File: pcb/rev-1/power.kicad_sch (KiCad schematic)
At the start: 38 parts, among them J1 12402012E212A, J2 S2B-PH-SM4-TB, J6 B2B-PH-K-S, SW1 EVQPUD02K, U1 NUF2042XV6T1G, U2 RT6160AWSC, U3 KTS1662EUW-TR, U4 BQ25150YFPR

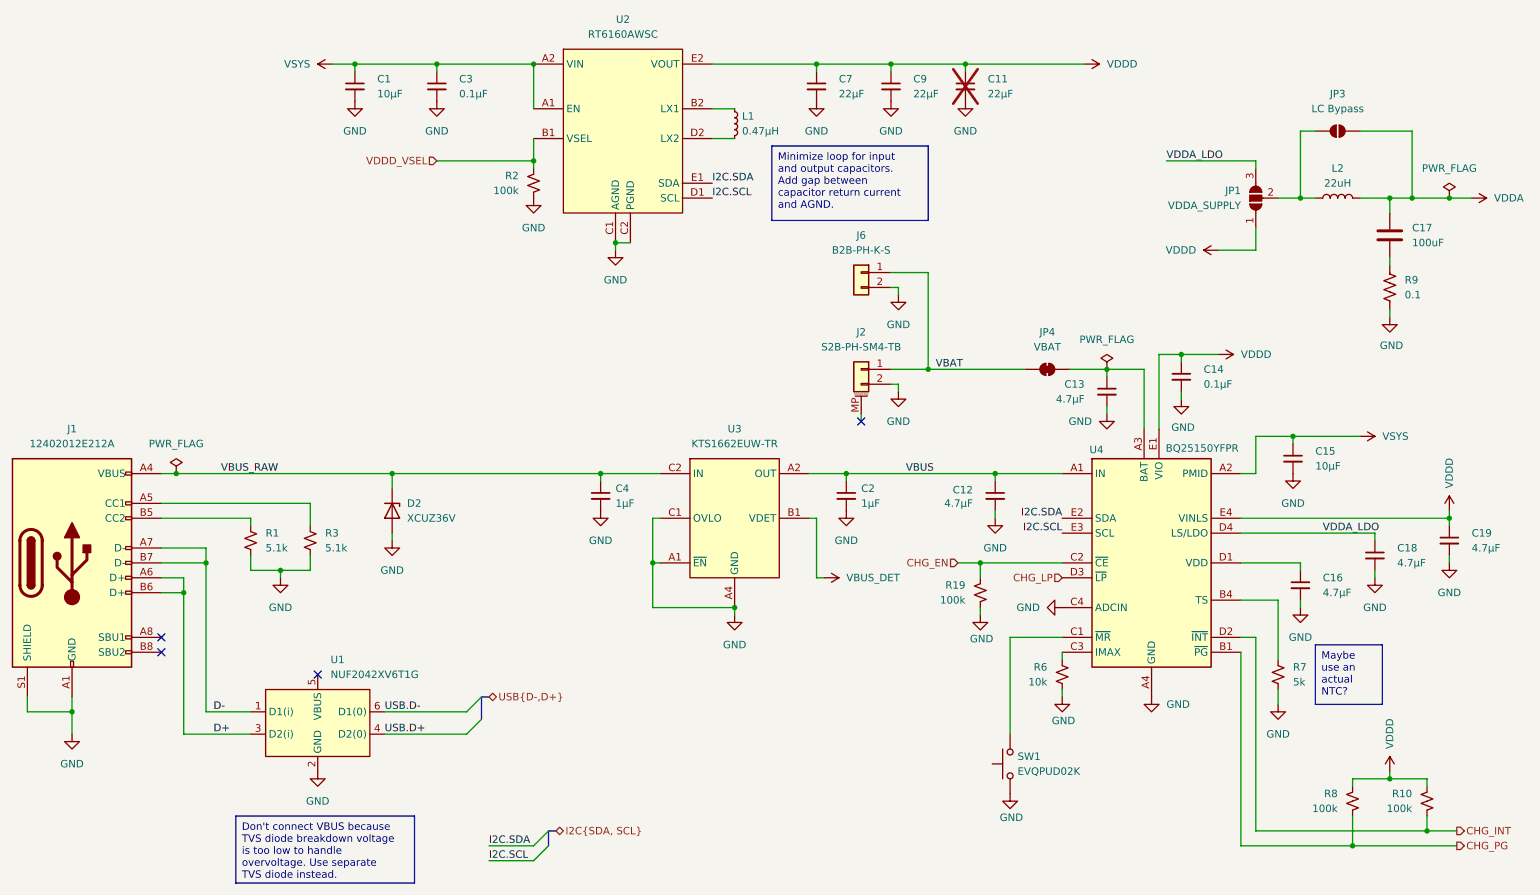
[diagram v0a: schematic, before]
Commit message: Update PCBs
* Update to KiCad 10
* Update footprint for nRF53 module based on 1.01 datasheet with
  actually readable mechanical drawing
* Add 3D model for production nRF53 module
* Remove overlapping silkscreen on rev-1 with production nRF53 module
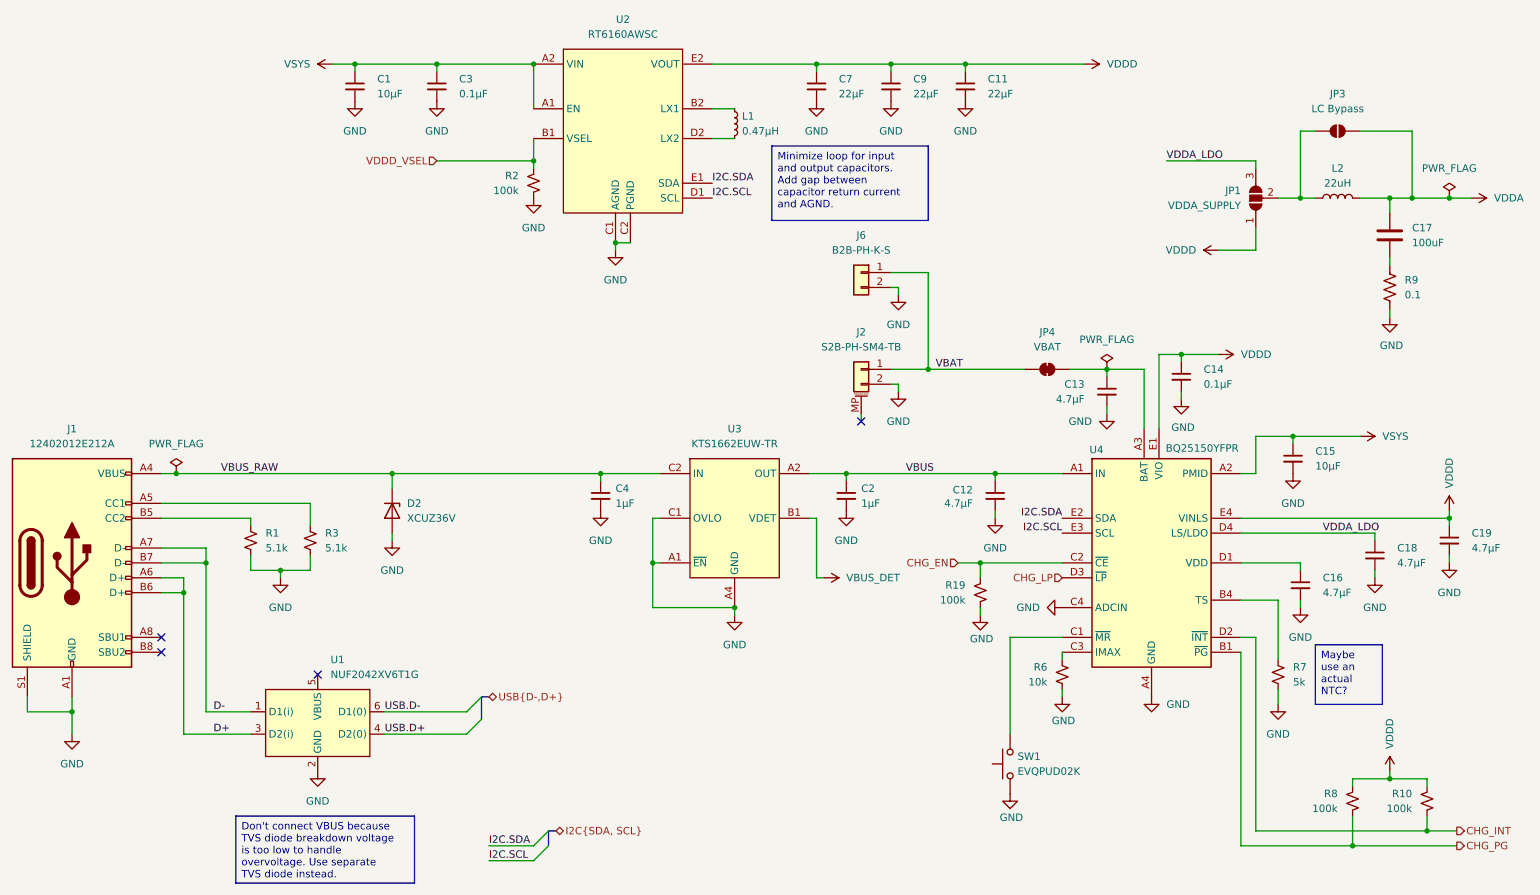
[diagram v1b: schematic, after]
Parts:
- C11: now fitted
